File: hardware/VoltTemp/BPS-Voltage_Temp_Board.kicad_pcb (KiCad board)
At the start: 4 copper layers, 98.4 x 81.3 mm, 149 parts, among them IC1 ISO1641BDR, J1 ScrutineeringConn, J10 53307-2471, J11 Conn_01x07, J3 Conn_01x05, J4 Conn_01x05, J5 Logic_Analyzer, J8 Conn_01x06, J9 Conn_01x03, T1 TP_TempOut, T2 TP_TempOut, T3 TP_TempOut, T4 TP_TempOut, T5 TP_TempOut, U1 EL3H7, U12 TLV9062xD, U13 TLV9062xD, U14 TLV9062xD, U2 BQ7692003PW, U3 EL3H7, U4 TLV9062xD, U6 TLV9062xD

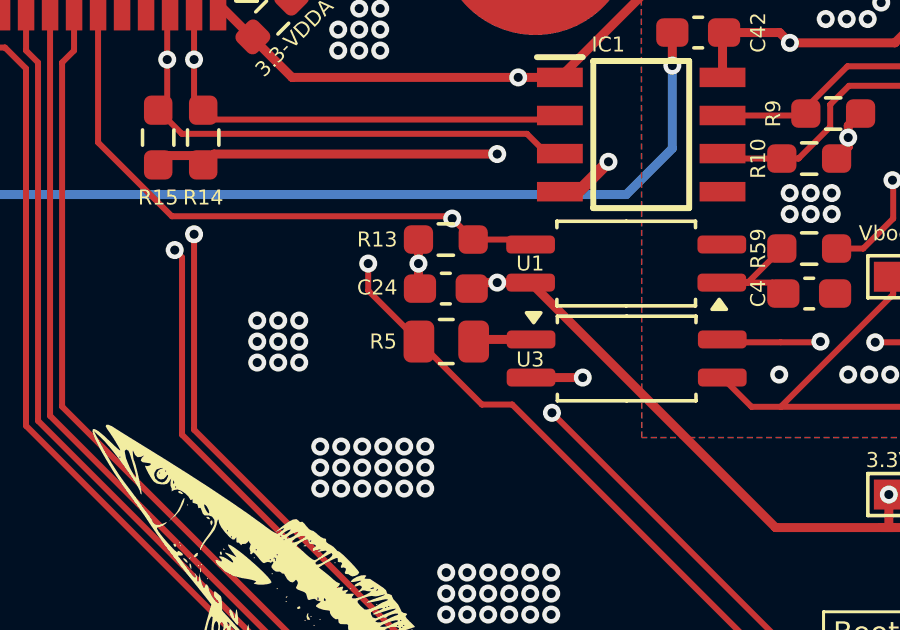
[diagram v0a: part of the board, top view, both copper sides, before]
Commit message: LCSC BOM & Validation square added
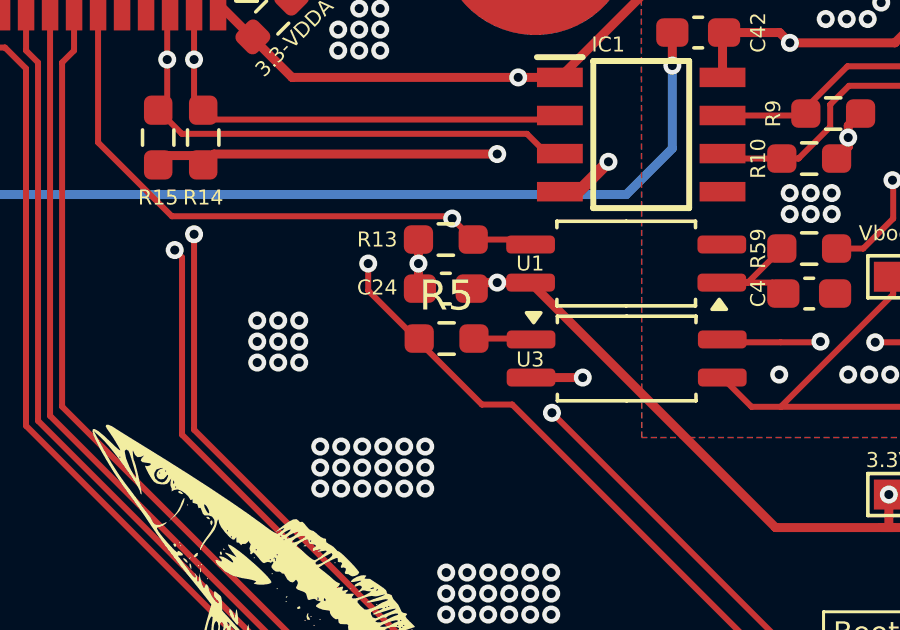
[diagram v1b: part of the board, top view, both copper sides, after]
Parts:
- R3: value 3.3kΩ -> 2kΩ
- R4: value 1kΩ -> 2kΩ
- R5: footprint Resistor_SMD:R_0805_2012Metric -> Resistor_SMD:R_0603_1608Metric_Pad0.98x0.95mm_HandSolder
- moved G*** 10.9 mm to (36.3, 77.0)
- moved R5 0.10 mm to (48.9, 61.6)
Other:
- board text added: "validated"
